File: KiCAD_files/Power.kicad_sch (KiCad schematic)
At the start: 62 parts, among them J11 Conn_01x01, J14 Conn_01x01, J17 Conn_01x01, J2 2604-1102, J20 Conn_01x01, J27 Conn_01x01, J28 Conn_01x01, J29 Conn_01x01, J3 Conn_01x01, J30 Conn_01x01, J32 Conn_01x01, J33 Conn_01x01, J34 Conn_01x01, J35 Conn_01x01, J4 2604-1102, J5 2604-1102, U13 OPA316, U3 ACS712xLCTR-20A, U5 AMC1311, U8 OPA316

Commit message: Added feeder project alpha version
Former-commit-id: 38773bad2925cccbdf57e9531d71dd427b0662b4
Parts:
- removed C38: 100nF, Capacitor_SMD:C_0805_2012Metric, symbol Device:C_Small
- removed F?: Nano2 fuse holder, Footprints:Fuse_holder_omni_blok, symbol Device:Fuse
- removed J?: 2604-1102, Footprints:WAGO-2604-1102, symbol Symbols:2604-1102
- added C103, C117: 20pF, Capacitor_SMD:C_0805_2012Metric, symbol Device:C_Small
- added C104: 100nF, Capacitor_SMD:C_0805_2012Metric, symbol Device:C_Small
- added R105, R110: 1k, Resistor_SMD:R_0805_2012Metric, symbol Device:R_Small
- R106: renamed from R21; value 200k -> 62k
- R107: renamed from R22; value 200k -> 43k
- R108: renamed from R25; value 82k -> 43k
- R109: renamed from R30; value 82k -> 62k
- gave numbers to parts that had none: 4
- renumbered C27 to C101, C37 to C102, C13 to C105, C14 to C106, C15 to C107, C16 to C108, C17 to C109, C18 to C110, C19 to C111, C20 to C112, C21 to C113, C23 to C114, C25 to C115, C26 to C116, C5 to C118, C32 to C119, C4 to C120, F1 to F103, F4 to F104, H3 to H101, H1 to H102, H4 to H103, HS1 to HS101, J2 to J103, J35 to J104, J32 to J105, J27 to J106, J28 to J107, J29 to J108, J3 to J109, J34 to J110, J11 to J111, J14 to J112, J30 to J113, J33 to J114, J17 to J115, J20 to J116, J5 to J117, J4 to J118, R7 to R101, R8 to R102, R13 to R103, R16 to R104, Rbleed1 to Rbleed101, Rbleed2 to Rbleed102, Rv5 to Rv101, Rv6 to Rv102, U5 to U101, U8 to U102, U13 to U103, U3 to U104
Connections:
- net +5VD: now also R105.1, R110.1; no longer C119.1, U103.5 (V+)
- net DGND: now also C104.2; no longer R107.1
- net IIHigh_op: now also C117.2
- net VIHigh_op: now also C103.2
- net Vref: now also R107.1
- net at R107.2, R109.1, U103.3 (-): now also C117.1
- net at R102.2, R104.1, U102.3 (-): now also C103.1
- new net U13_5V: C119.1, R110.2, U103.5 (V+)
- new net U8_5V: C104.1, R105.2
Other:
- removed sheet Power Leg 3
- note added: "V_{SHIFTED} = ((R109 + R107)*R3 / (R106 + R108)*R107) * I_{IHigh} - (R109/R107)* V_{ref}"
- note added: "V_{SHIFTED} = I_{IHigh} - (62K/43K)* V_{ref}"
- note added: "V_{SHIFTED} = I_{IHigh} - 1.5V"
- moved on the sheet: C101, C102, C105, C106, C107, C108, C109, C110, C111, C112, C113, C114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

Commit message: WIP routing the power board
Former-commit-id: fec71ccccc2062c429ca6048755d91568543f1a5
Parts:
- removed H101, H103: MountingHole_Pad, MountingHole:MountingHole_2.2mm_M2_ISO7380_Pad, symbol Mechanical:MountingHole_Pad
- removed H102: MountingHole, Footprints:mounting_holes, symbol Mechanical:MountingHole
- added R23, R24, R29: 1k, Resistor_SMD:R_0805_2012Metric, symbol Device:R_Small
- F101, F102, F103, F104: value Nano2 fuse holder -> 8A
- U101: footprint Footprints:SOIC-8_7.5x5.85mm_P1.27mm -> Package_SO:SOIC-8_7.5x5.85mm_P1.27mm
- U104: value ACS712xLCTR-20A -> +-20A; symbol Sensor_Current:ACS712xLCTR-20A -> Symbols:ACS723
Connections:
- net +5P: now also R29.1; no longer C101.1, U101.1 (VDD1)
- net +5VD: now also R23.1, R24.1; no longer C102.1, C120.2, U101.8 (VDD2), U102.5 (V+), U104.8 (VCC)
- net N renamed NGND
- net Power Leg 1/I_High renamed Power Leg 1/V_High
- net Power Leg 1/VI_LOW1 renamed V1_Low
- net Power Leg 2/VI_LOW2 renamed V2_Low
- net U13_5V: no longer names the net of C119.1, R110.2, U103.5 (V+)
- net U8_5V: no longer names the net of C104.1, R105.2
- net U8_5V: now also U102.5 (V+)
- net Vref renamed VRef
- new net: C120.2, R24.2, U104.8 (VCC)
- new net: C101.1, R29.2, U101.1 (VDD1)
- new net: C102.1, R23.2, U101.8 (VDD2)
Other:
- sheet Power Leg 1 ports: added V_High, V_Low; removed I_High, VI_LOW1
- sheet Power Leg 2: file PowerLeg2.kicad_sch -> PowerLeg1.kicad_sch
- sheet Power Leg 2 ports: added V_High, V_Low; removed I_High, VI_LOW2
- note removed: "M2.5 pass through holes for thermistor sensor"
- note removed: "Thermal jumpers connecting the mosfets and diode to the heatsink with electrical insulation"
- moved on the sheet: C101, C102, C103, C104, C117, C118, C119, C120, F101, F102, J101, J102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

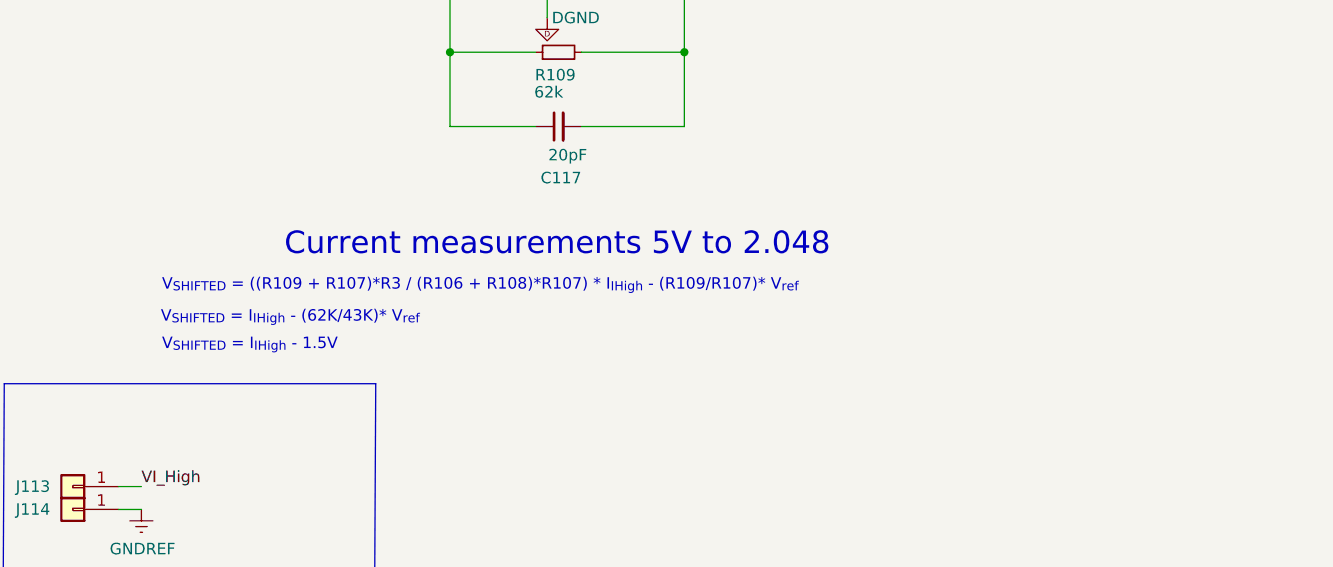
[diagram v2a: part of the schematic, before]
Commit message: Edited opamp comments that were outdated.
Former-commit-id: 22e139dd8e717e45edbeb5b70fb47a644a62ae14
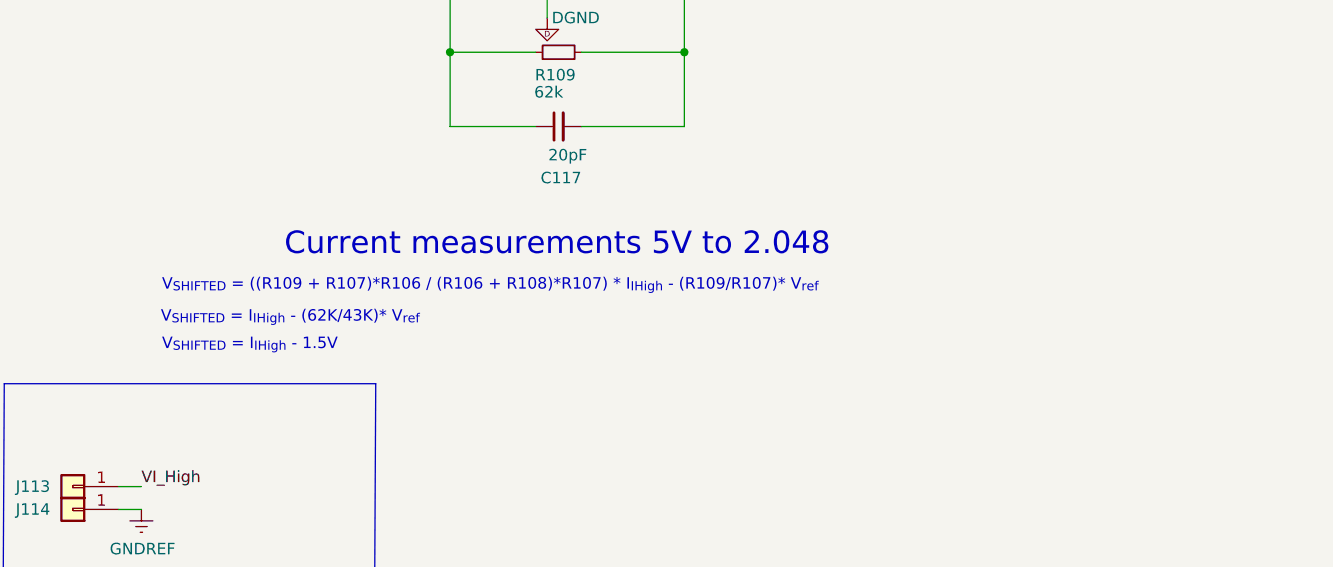
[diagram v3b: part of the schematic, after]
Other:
- note added: "V_{SHIFTED} = ((R109 + R107)*R106 / (R106 + R108)*R107) * I_{IHigh} - (R109/R107)* V_{ref}"
- note removed: "V_{SHIFTED} = ((R109 + R107)*R3 / (R106 + R108)*R107) * I_{IHigh} - (R109/R107)* V_{ref}"
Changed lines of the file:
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@@
     (effects (font (size 2.4892 2.4892)) (justify left bottom))
   )
-  (text "V_{SHIFTED} = ((R109 + R107)*R3 / (R106 + R108)*R107) * I_{IHigh} - (R109/R107)* V_{ref}"
+  (text "V_{SHIFTED} = ((R109 + R107)*R106 / (R106 + R108)*R107) * I_{IHigh} - (R109/R107)* V_{ref}"
     (at 195.326 228.6 0)
     (effects (font (size 1.27 1.27)) (justify left bottom))
